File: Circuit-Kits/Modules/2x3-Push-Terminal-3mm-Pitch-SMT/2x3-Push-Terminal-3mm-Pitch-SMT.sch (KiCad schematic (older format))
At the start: 0 parts

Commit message: Add 2x2 and 2x3 Pushbutton schematics and parts.
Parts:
- added J1: Push Terminal Block, symbol Conn_2
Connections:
- new net 1: J1.1
- new net 2: J1.2
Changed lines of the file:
@@
 Comment4 ""
 $EndDescr
+$Comp
+L Conn_2 J1
+U 1 1 587EB9D9
+P 4950 3575
+F 0 "J1" H 4900 3700 50  0000 L CNN
+F 1 "Push Terminal Block" H 4900 3450 50  0000 L CNN
+F 2 "" H 4950 3575 50  0000 C CNN
+F 3 "" H 4950 3575 50  0000 C CNN
+F 4 "Molex" H 4950 3575 60  0001 C CNN "MF_Name"
+F 5 "1042380210" H 4950 3575 60  0001 C CNN "MF_PN"
+F 6 "Digikey" H 4950 3575 60  0001 C CNN "S1_Name"
+F 7 "WM11924CT-ND" H 4950 3575 60  0001 C CNN "S1_PN"
+F 8 "CONN MINI LITE-TRAP RCPT 2POS" H 4950 3575 60  0001 C CNN "Description"
+	1    4950 3575
+	1    0    0    -1
+$EndComp
+Wire Wire Line
+	5100 3525 5225 3525
+Wire Wire Line
+	5100 3600 5225 3600
+Text Label 5225 3525 2    50   ~ 0
+1
+Text Label 5225 3600 2    50   ~ 0
+2
 $EndSCHEMATC

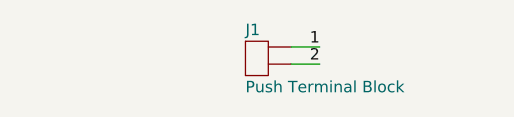
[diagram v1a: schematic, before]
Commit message: Releave v1.0 2x3, 2x2 Push Terminals.
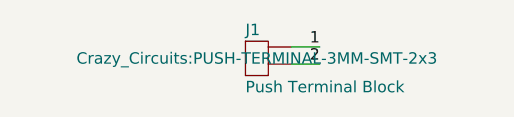
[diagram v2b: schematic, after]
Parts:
- J1: footprint (none) -> Crazy_Circuits:PUSH-TERMINAL-3MM-SMT-2x3
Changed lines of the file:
@@
 Title "2x3 Push Terminal 3mm Pitch SMT"
 Date "17 Mar 2017"
-Rev"1.0"
-Comp "All rights reserved.")
-Comment1 "help@browndoggadgets.com")
-Comment2 "http://browndoggadgets.com/")
-Comment3 "Brown Dog Gadgets")
+Rev "1.0"
+Comp "All rights reserved."
+Comment1 "help@browndoggadgets.com"
+Comment2 "http://browndoggadgets.com/"
+Comment3 "Brown Dog Gadgets"
 Comment4 ""
 $EndDescr
@@
 F 0 "J1" H 4900 3700 50  0000 L CNN
 F 1 "Push Terminal Block" H 4900 3450 50  0000 L CNN
-F 2 "" H 4950 3575 50  0000 C CNN
+F 2 "Crazy_Circuits:PUSH-TERMINAL-3MM-SMT-2x3" H 4950 3575 50  0000 C CNN
 F 3 "" H 4950 3575 50  0000 C CNN
 F 4 "Molex" H 4950 3575 60  0001 C CNN "MF_Name"
